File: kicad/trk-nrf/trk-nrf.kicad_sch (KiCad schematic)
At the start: 42 parts, among them U1 nRF9151-LAXX, U2 CDCE6214RGER, U3 TPS631010YBGR, U4 TPS631010YBGR, X1 TG2520SMN-xx.xxxxxxMhz-xxxxNM

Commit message: Updates - pre-routing
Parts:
- added J1: Conn_02x05_Odd_Even, Connector_PinHeader_1.00mm:PinHeader_2x05_P1.00mm_Vertical_SMD, symbol Connector_Generic:Conn_02x05_Odd_Even
- C1: footprint Capacitor_SMD:C_1206_3216Metric -> Capacitor_SMD:C_0805_2012Metric
- R11: footprint Resistor_SMD:R_0603_1608Metric -> Resistor_SMD:R_0402_1005Metric
- TP1, TP2: footprint TestPoint:TestPoint_THTPad_D2.5mm_Drill1.2mm -> TestPoint:TestPoint_Pad_1.5x1.5mm
- TP3: value WSPR N -> WSPR_ANT_N
- TP4: value WSPR P -> WSPR _ANT_P
- TP5, TP6: footprint TestPoint:TestPoint_THTPad_D2.5mm_Drill1.2mm -> TestPoint:TestPoint_THTPad_D1.5mm_Drill0.7mm
- U3, U4: footprint footprints:YBG0008-MFG -> footprints:YBG0008
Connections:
- net GND: now also J1.1 (Pin_1)
- net MON_V3P3: now also R14.2
- net SCL: now also J1.4 (Pin_4)
- net SDA: now also J1.2 (Pin_2)
- net SWDCLK: now also J1.3 (Pin_3)
- net SWDIO: now also J1.5 (Pin_5)
- net TCXO_REFCLK: no longer U2.5 (PRIREF_P), X1.3 (OUT)
- net UART_RX: now also J1.6 (Pin_6)
- net UART_TX: now also J1.8 (Pin_8)
- net +3.3V_Ferrite: now reaches C10.1, C9.1, L3.2, U1.10 (ENABLE), U1.14 (VDD)
- net 1PPS: now reaches U1.53 (COEX1)
- net 1PPS: now also U1.64 (P0.07), J1.10 (Pin_10)
- net nRF_nRESET: now reaches C6.1, U1.9 (~{RESET})
- net FB_1.8: now reaches R1.2, R2.1, U3.D2 (FB)
- net FB_3.3: now reaches R3.2, R4.1, U4.D2 (FB)
- new net: U2.5 (PRIREF_P), X1.3 (OUT)
- new net +1.8V: J1.9 (Pin_9)
- new net nrf_nRESET: J1.7 (Pin_7)
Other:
- moved on the sheet: C7, C8, R9, TP3, TP4, X1

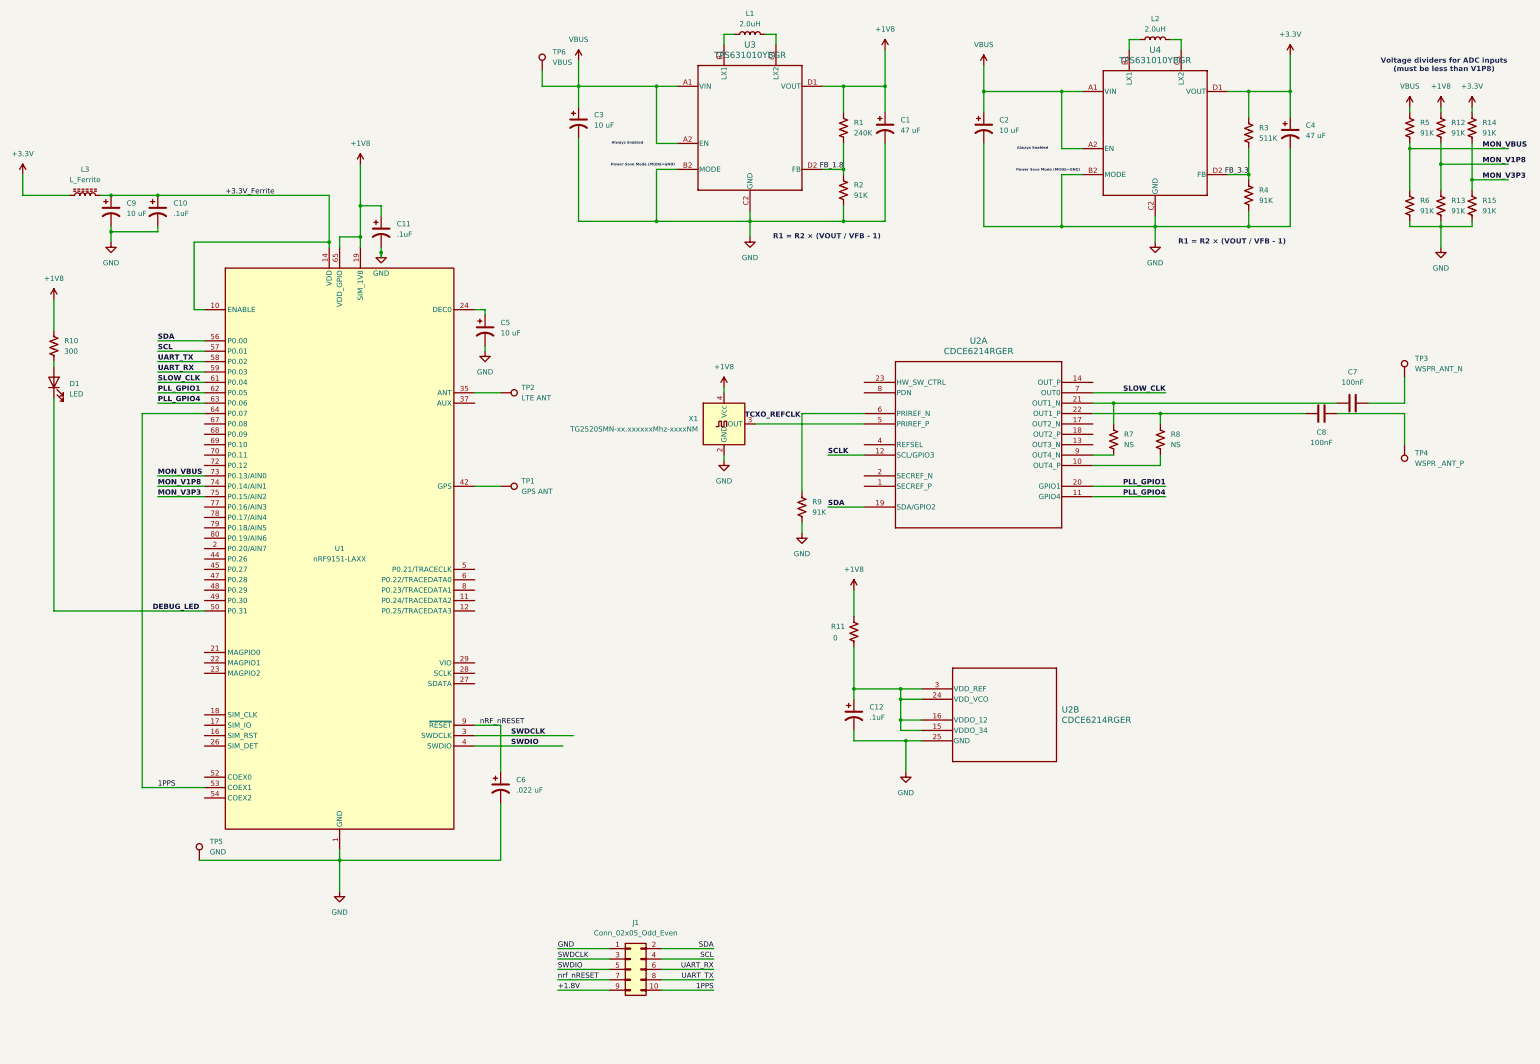
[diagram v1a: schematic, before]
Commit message: Schematic edits and drc changes
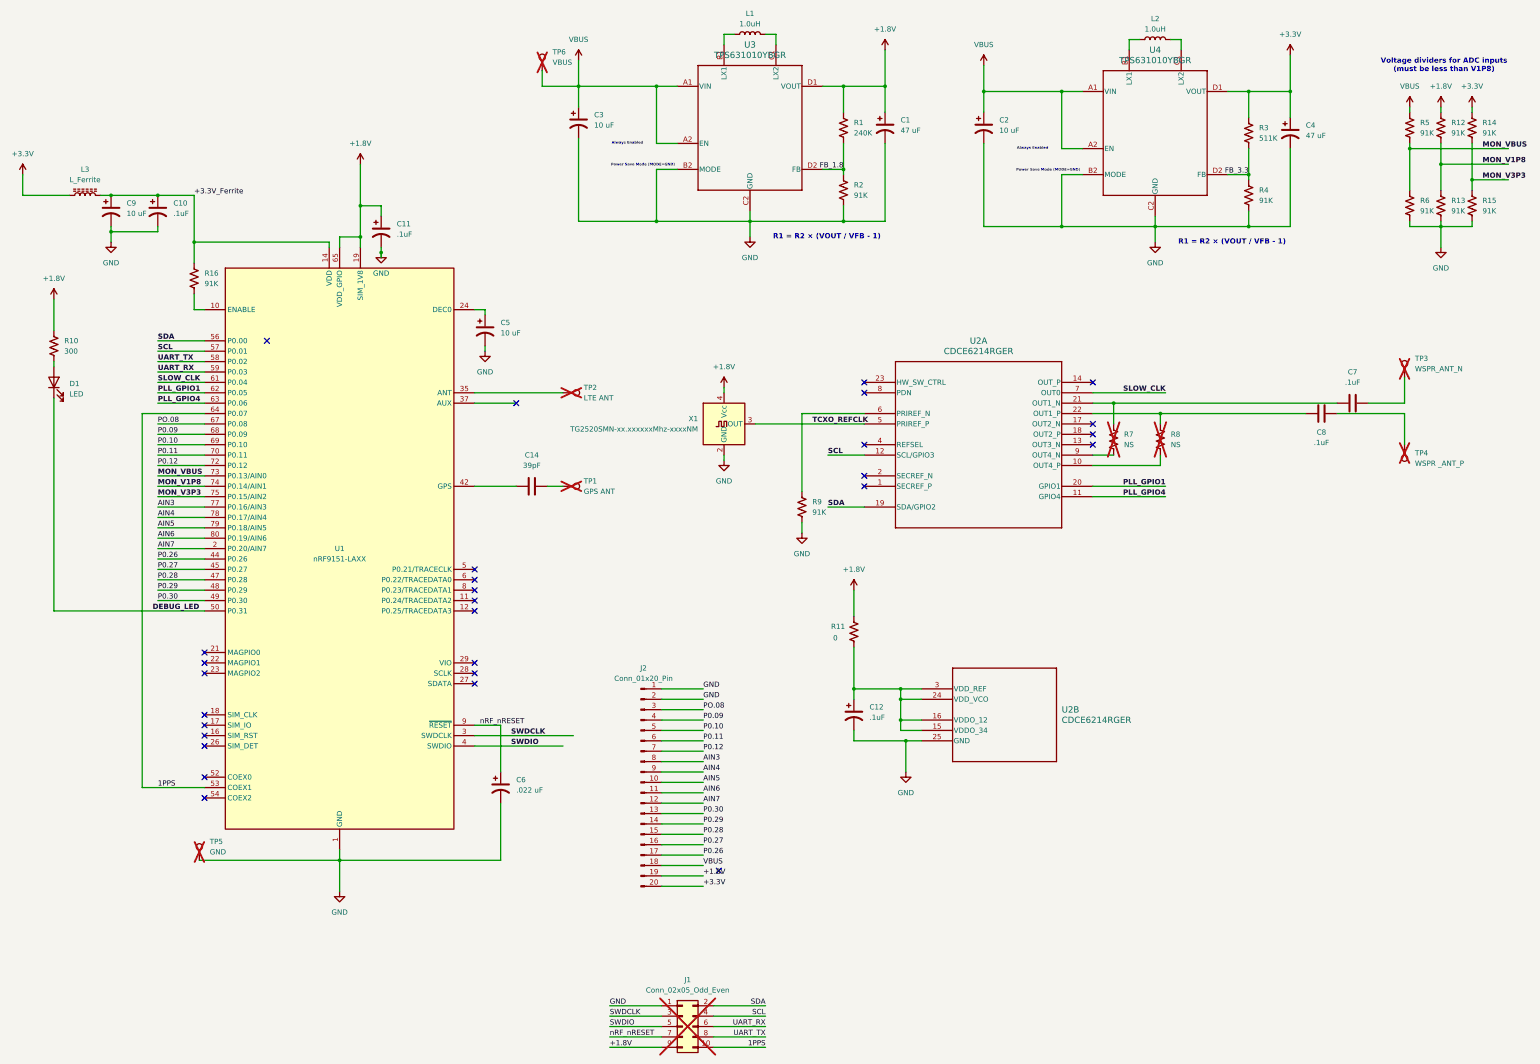
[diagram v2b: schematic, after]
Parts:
- added C14: 39pF, Capacitor_SMD:C_0402_1005Metric, symbol Device:C
- added J2: Conn_01x20_Pin, Connector_FFC-FPC:Hirose_FH12-20S-0.5SH_1x20-1MP_P0.50mm_Horizontal, symbol Connector:Conn_01x20_Pin
- added R16: 91K, Resistor_SMD:R_0402_1005Metric, symbol Device:R_US
- C1: JLCPCB Part Number (none) -> C16780
- C10, C11, C12: JLCPCB Part Number (none) -> C1525
- C2, C3, C5, C9: JLCPCB Part Number (none) -> C1691
- C4: footprint Capacitor_SMD:C_1206_3216Metric -> Capacitor_SMD:C_0805_2012Metric; JLCPCB Part Number (none) -> C16780
- C6: JLCPCB Part Number (none) -> C60474
- C7, C8: value 100nF -> .1uF; JLCPCB Part Number (none) -> C1525
- D1, X1: JLCPCB Part Number (none) -> C3007519
- J1, R7, R8, TP1, TP2, TP3, TP4, TP5, TP6: now not fitted
- L1, L2: value 2.0uH -> 1.0uH; footprint Inductor_SMD:L_0805_2012Metric -> Inductor_SMD:L_Murata_DFE201610P; JLCPCB Part Number (none) -> C92921
- L3: JLCPCB Part Number (none) -> C12389
- R1: JLCPCB Part Number (none) -> C64043
- R10: JLCPCB Part Number (none) -> C25159
- R11: JLCPCB Part Number (none) -> C17168
- R12, R13, R14, R15, R2, R4, R5, R6, R9: JLCPCB Part Number (none) -> C25573
- R3: JLCPCB Part Number (none) -> C64042
- U1: JLCPCB Part Number (none) -> C22397843
- U2: JLCPCB Part Number (none) -> C3608351
- U3, U4: JLCPCB Part Number (none) -> C6719123
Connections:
- net +1V8 is gone; now on net +1.8V: C1.1, C11.1, R1.1, R10.1, R11.1, R12.1, U1.19 (SIM_1V8), U1.65 (VDD_GPIO), U3.D1 (VOUT), X1.4 (Vcc)
- net SCLK is gone; now on net SCL: U2.12 (SCL/GPIO3)
- net nrf_nRESET is gone; now on net nRF_nRESET: J1.7 (Pin_7)
- net +1.8V: now also J2.19 (Pin_19)
- net +3.3V: now also J2.20 (Pin_20)
- net +3.3V_Ferrite: now also R16.1; no longer U1.10 (ENABLE)
- net GND: now also J2.1 (Pin_1), J2.2 (Pin_2)
- net TCXO_REFCLK: now also U2.5 (PRIREF_P), X1.3 (OUT)
- net VBUS: now also J2.18 (Pin_18)
- net AIN7: now reaches U1.2 (P0.20/AIN7)
- net AIN7: now also J2.12 (Pin_12)
- net at U1.42 (GPS): now also C14.1; no longer TP1.1
- net P0.26: now reaches U1.44 (P0.26)
- net P0.26: now also J2.17 (Pin_17)
- net P0.27: now reaches U1.45 (P0.27)
- net P0.27: now also J2.16 (Pin_16)
- net P0.28: now reaches U1.47 (P0.28)
- net P0.28: now also J2.15 (Pin_15)
- net P0.29: now reaches U1.48 (P0.29)
- net P0.29: now also J2.14 (Pin_14)
- net P0.30: now reaches U1.49 (P0.30)
- net P0.30: now also J2.13 (Pin_13)
- net PO.08: now reaches U1.67 (P0.08)
- net PO.08: now also J2.3 (Pin_3)
- net P0.09: now reaches U1.68 (P0.09)
- net P0.09: now also J2.4 (Pin_4)
- net P0.10: now reaches U1.69 (P0.10)
- net P0.10: now also J2.5 (Pin_5)
- net P0.11: now reaches U1.70 (P0.11)
- net P0.11: now also J2.6 (Pin_6)
- net P0.12: now reaches U1.72 (P0.12)
- net P0.12: now also J2.7 (Pin_7)
- net AIN3: now reaches U1.77 (P0.16/AIN3)
- net AIN3: now also J2.8 (Pin_8)
- net AIN4: now reaches U1.78 (P0.17/AIN4)
- net AIN4: now also J2.9 (Pin_9)
- net AIN5: now reaches U1.79 (P0.18/AIN5)
- net AIN5: now also J2.10 (Pin_10)
- net AIN6: now reaches U1.80 (P0.19/AIN6)
- net AIN6: now also J2.11 (Pin_11)
- new net: R16.2, U1.10 (ENABLE)
- new net: C14.2, TP1.1
- no-connect marks 0 -> 29

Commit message: Updated schematic
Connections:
- net AIN7 is gone; now on net MON_VBUS: J2.12 (Pin_12), U1.2 (P0.20/AIN7)
- net MON_VBUS: no longer U1.73 (P0.13/AIN0)
- new net AIN0: U1.73 (P0.13/AIN0)
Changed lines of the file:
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@@
+		)
+	)
+	(label "MON_VBUS"
+		(at 52.07 144.78 0)
+		(fields_autoplaced yes)
+		(effects
+			(font
+				(size 1.27 1.27)
+				(thickness 0.254)
+				(bold yes)
+			)
+			(justify left bottom)
 		)
 	)
@@
 		)
 	)
-	(label "MON_VBUS"
-		(at 52.07 127 0)
-		(fields_autoplaced yes)
-		(effects
-			(font
-				(size 1.27 1.27)
-				(thickness 0.254)
-				(bold yes)
-			)
-			(justify left bottom)
-		)
-	)
 	(label "+3.3V_Ferrite"
 		(at 60.96 58.42 0)
@@
 		)
 	)
-	(label "AIN7"
-		(at 52.07 144.78 0)
-		(fields_autoplaced yes)
-		(effects
-			(font
-				(size 1.27 1.27)
-			)
-			(justify left bottom)
-		)
-	)
 	(label "UART_RX"
 		(at 200.66 261.62 180)
@@
 		)
 	)
-	(label "AIN7"
+	(label "MON_VBUS"
 		(at 185.42 207.01 0)
 		(fields_autoplaced yes)
@@
 		(fields_autoplaced yes)
 		(effects
+			(font
+				(size 1.27 1.27)
+			)
+			(justify left bottom)
+		)
+	)
+	(label "AIN0"
+		(at 52.07 127 0)
+		(fields_autoplaced yes)
+		(effects

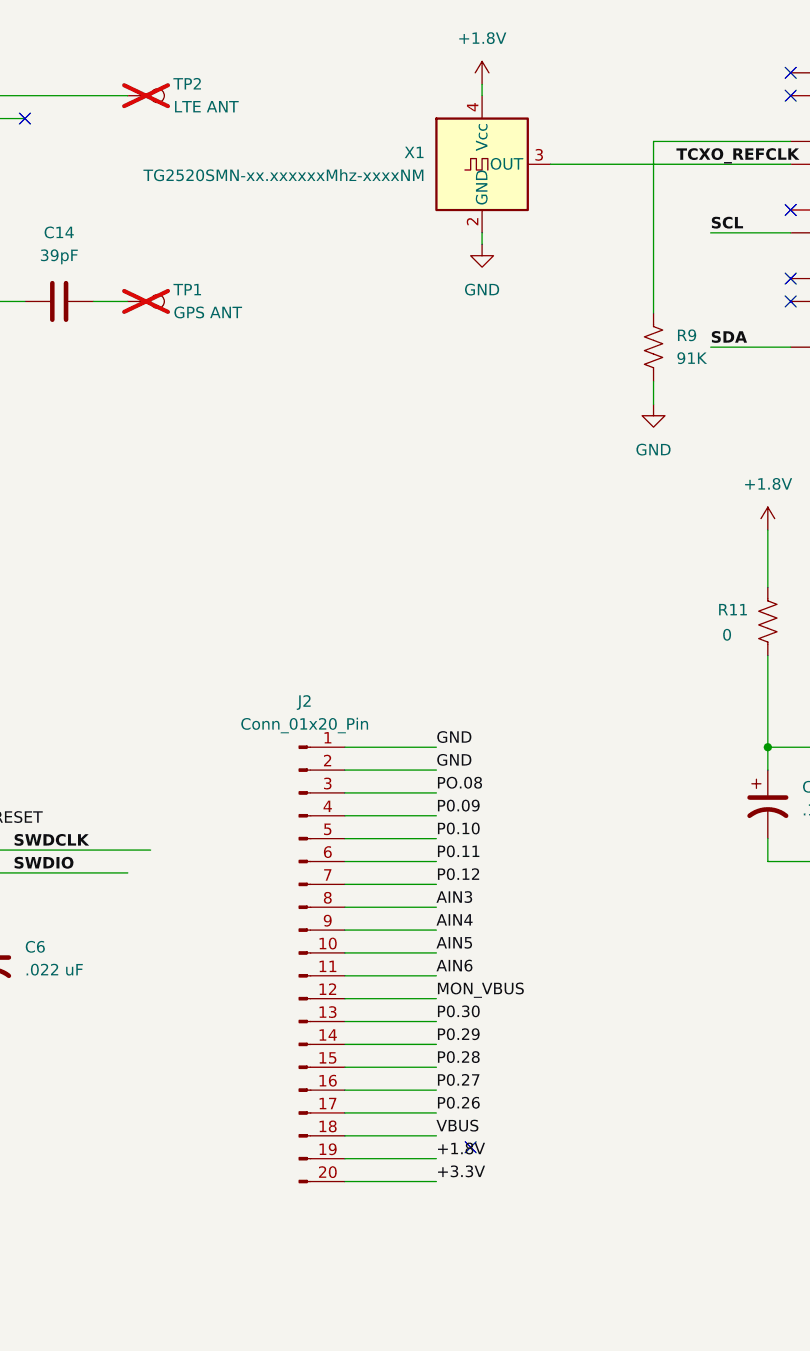
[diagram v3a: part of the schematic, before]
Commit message: Add second ground and freeroute board
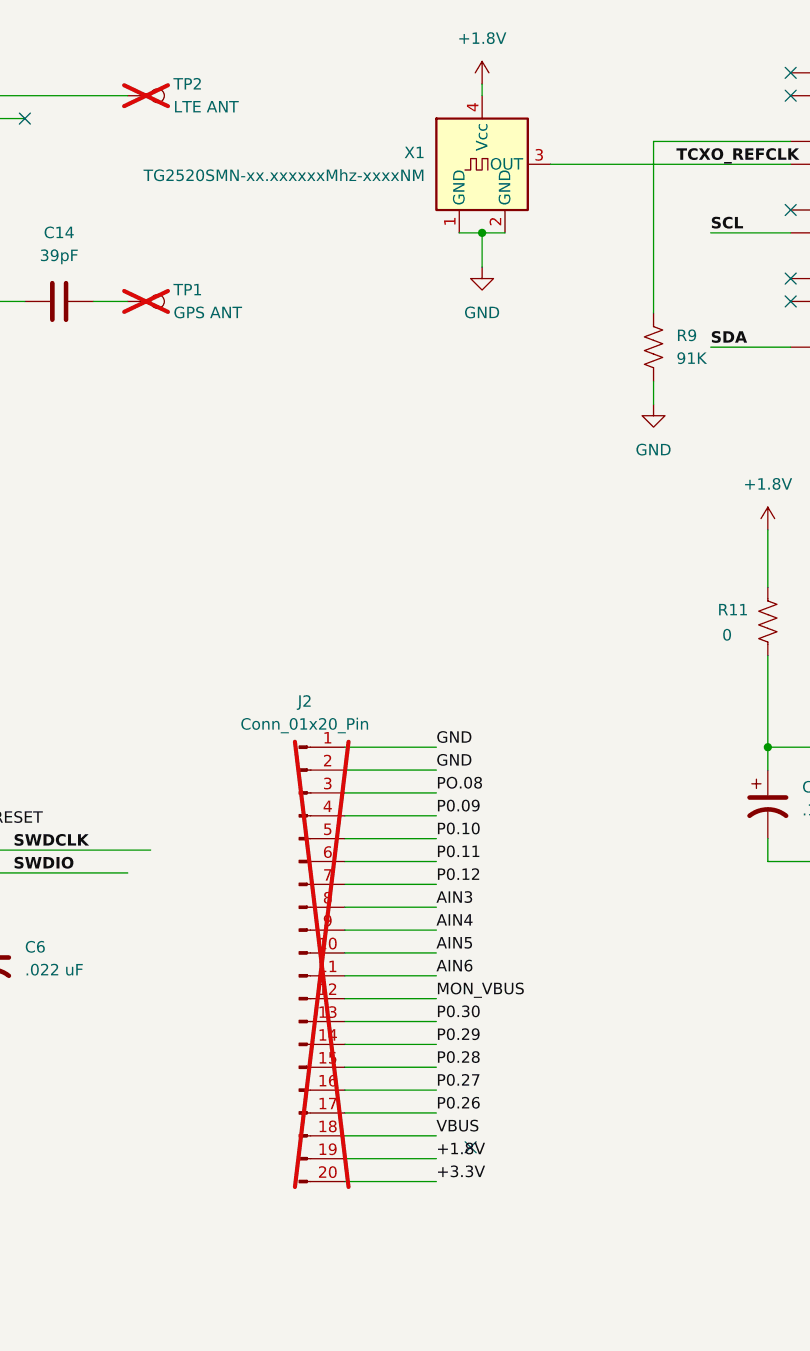
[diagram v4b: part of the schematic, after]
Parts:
- J2: now not fitted
- X1: JLCPCB Part Number C3007519 -> C5590921
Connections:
- net GND: now also X1.1 (NC)
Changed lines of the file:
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@@
 	)
 	(junction
+		(at 190.5 121.92)
+		(diameter 0)
+		(color 0 0 0 0)
+	)
+	(junction
 		(at 318.77 33.02)
 		(diameter 0)
@@
 	(wire
 		(pts
+			(xy 190.5 121.92) (xy 193.04 121.92)
+		)
+		(stroke
+			(width 0)
+			(type default)
+		)
+	)
+	(wire
+		(pts
 			(xy 179.07 52.07) (xy 173.99 52.07)
 		)
@@
 	(wire
 		(pts
-			(xy 190.5 121.92) (xy 190.5 123.19)
+			(xy 190.5 121.92) (xy 190.5 125.73)
 		)
 		(stroke
@@
 	(wire
 		(pts
+			(xy 187.96 121.92) (xy 190.5 121.92)
+		)
+		(stroke
+			(width 0)
+			(type default)
+		)
+	)
+	(wire
+		(pts
 			(xy 273.05 33.02) (xy 273.05 46.99)
 		)
@@
 		(in_bom yes)
 		(on_board yes)
-		(dnp no)
+		(dnp yes)
 		(property "Reference" "J2"
 			(at 170.815 173.99 0)
@@
 			)
 		)
-		(property "Datasheet" "https://support.epson.biz/td/api/doc_check.php?dl=app_TG2520SMN&lang=en"
+		(property "Datasheet" "https://wmsc.lcsc.com/wmsc/upload/file/pdf/v2/lcsc/2311291321_Abracon-LLC-ATX-12-F-26-000MHZ-F05-T_C5590921.pdf"
 			(at 187.96 114.3 0)
 			(effects
@@
 			)
 		)
-		(property "JLCPCB Part Number" "C3007519"
+		(property "JLCPCB Part Number" "C5590921"
 			(at 190.5 114.3 0)
 			(effects
@@
 		(pin "4"
 		)
+		(pin "1"
+		)
 		(instances
 			(project ""
@@
 	(symbol
 		(lib_id "power:GND")
-		(at 190.5 123.19 0)
+		(at 190.5 125.73 0)
 		(unit 1)
 		(exclude_from_sim no)
@@
 		(fields_autoplaced yes)
 		(property "Reference" "#PWR019"
-			(at 190.5 129.54 0)
+			(at 190.5 132.08 0)
 			(effects
 				(font
@@
 		)
 		(property "Value" "GND"
-			(at 190.5 128.27 0)
+			(at 190.5 130.81 0)
 			(effects
 				(font
@@
 		)
 		(property "Footprint" ""
-			(at 190.5 123.19 0)
+			(at 190.5 125.73 0)
 			(effects
 				(font
@@
 		)
 		(property "Datasheet" ""
-			(at 190.5 123.19 0)
+			(at 190.5 125.73 0)
 			(effects
 				(font
@@
 		)
 		(property "Description" "Power symbol creates a global label with name \"GND\" , ground"
-			(at 190.5 123.19 0)
+			(at 190.5 125.73 0)
 			(effects
 				(font
